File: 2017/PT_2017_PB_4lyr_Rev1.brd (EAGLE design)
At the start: 158.7 x 209.5 mm, 150 parts, among them Q12 2N7002

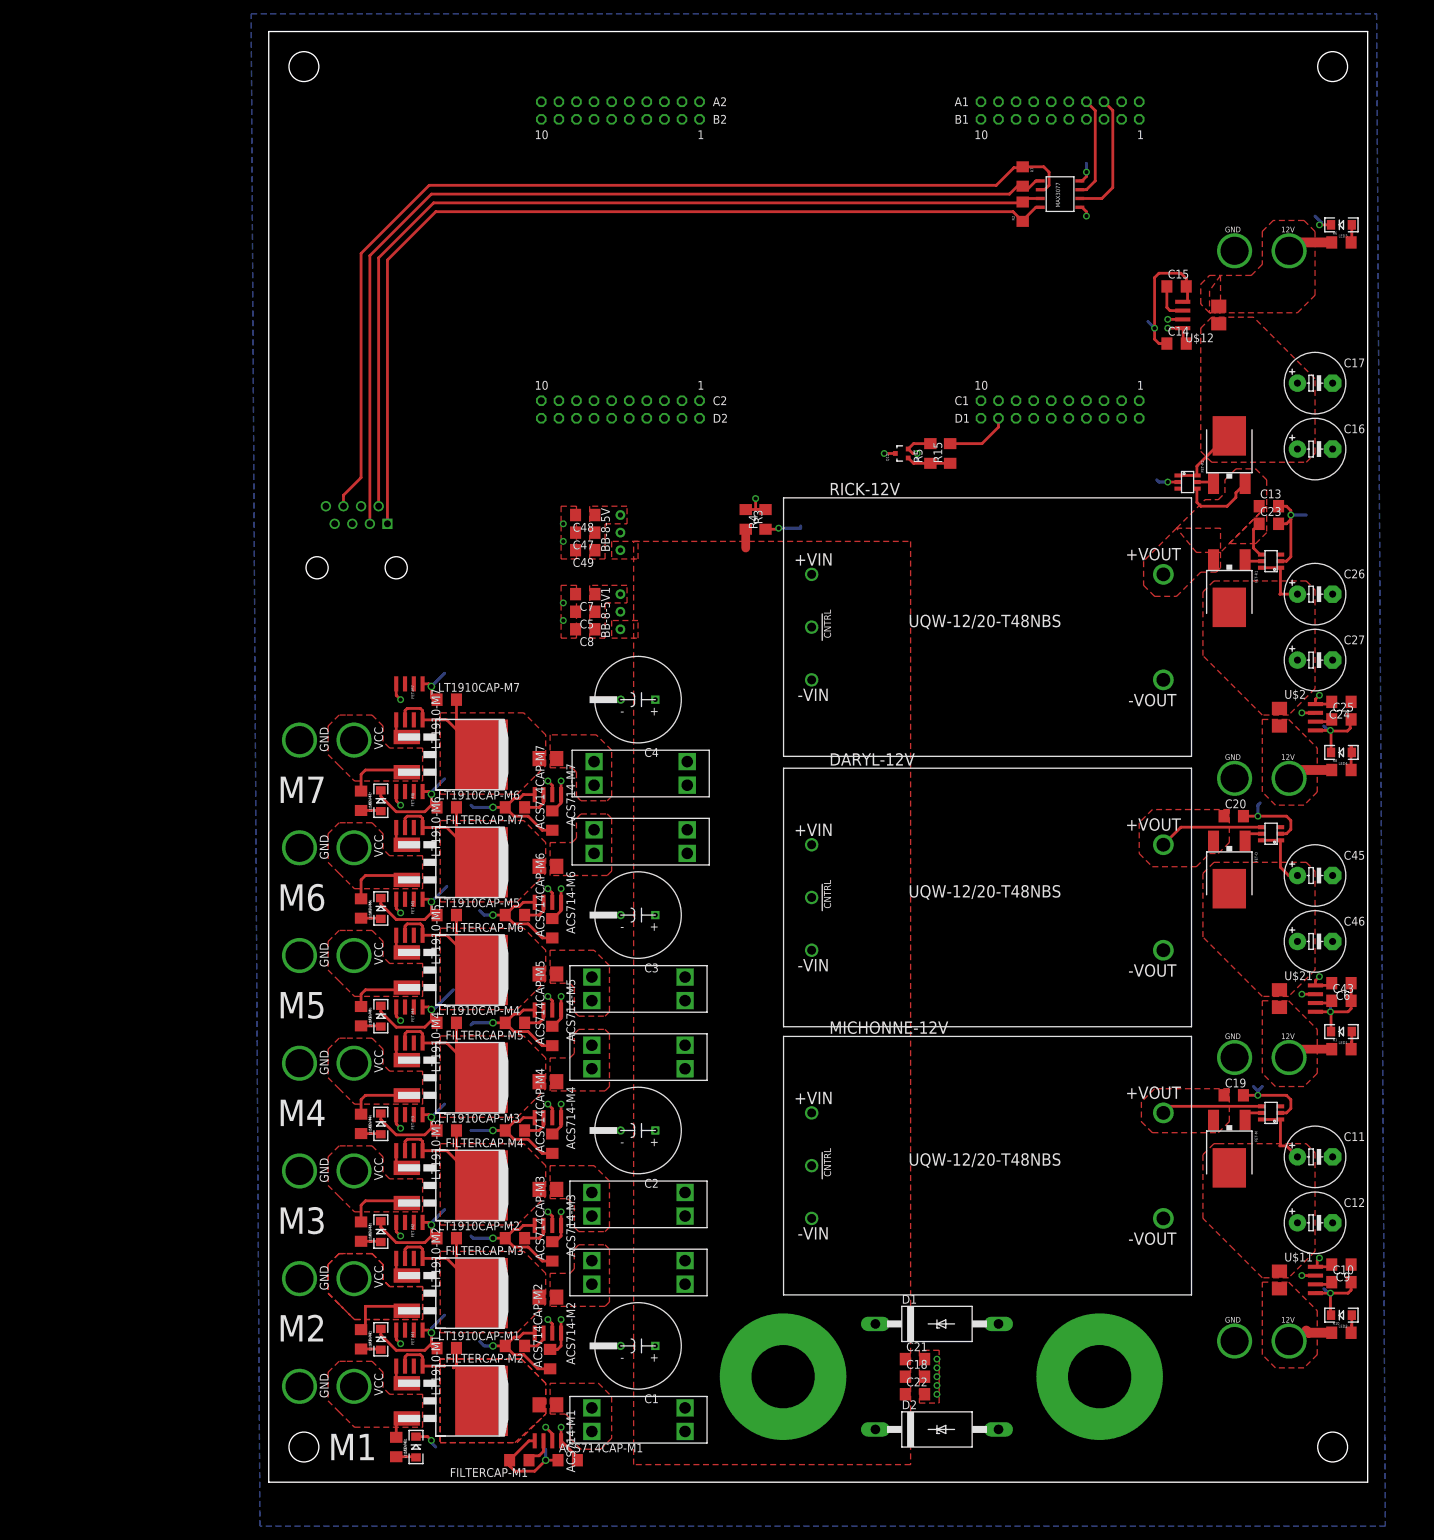
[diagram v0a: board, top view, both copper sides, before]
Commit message: Added fuse blocks and bus bar mounting holes
Fuse blocks for the 12V buses. Swapped temporary anderson connectors
with holes to mount bus bars to connect PB to patch panel.
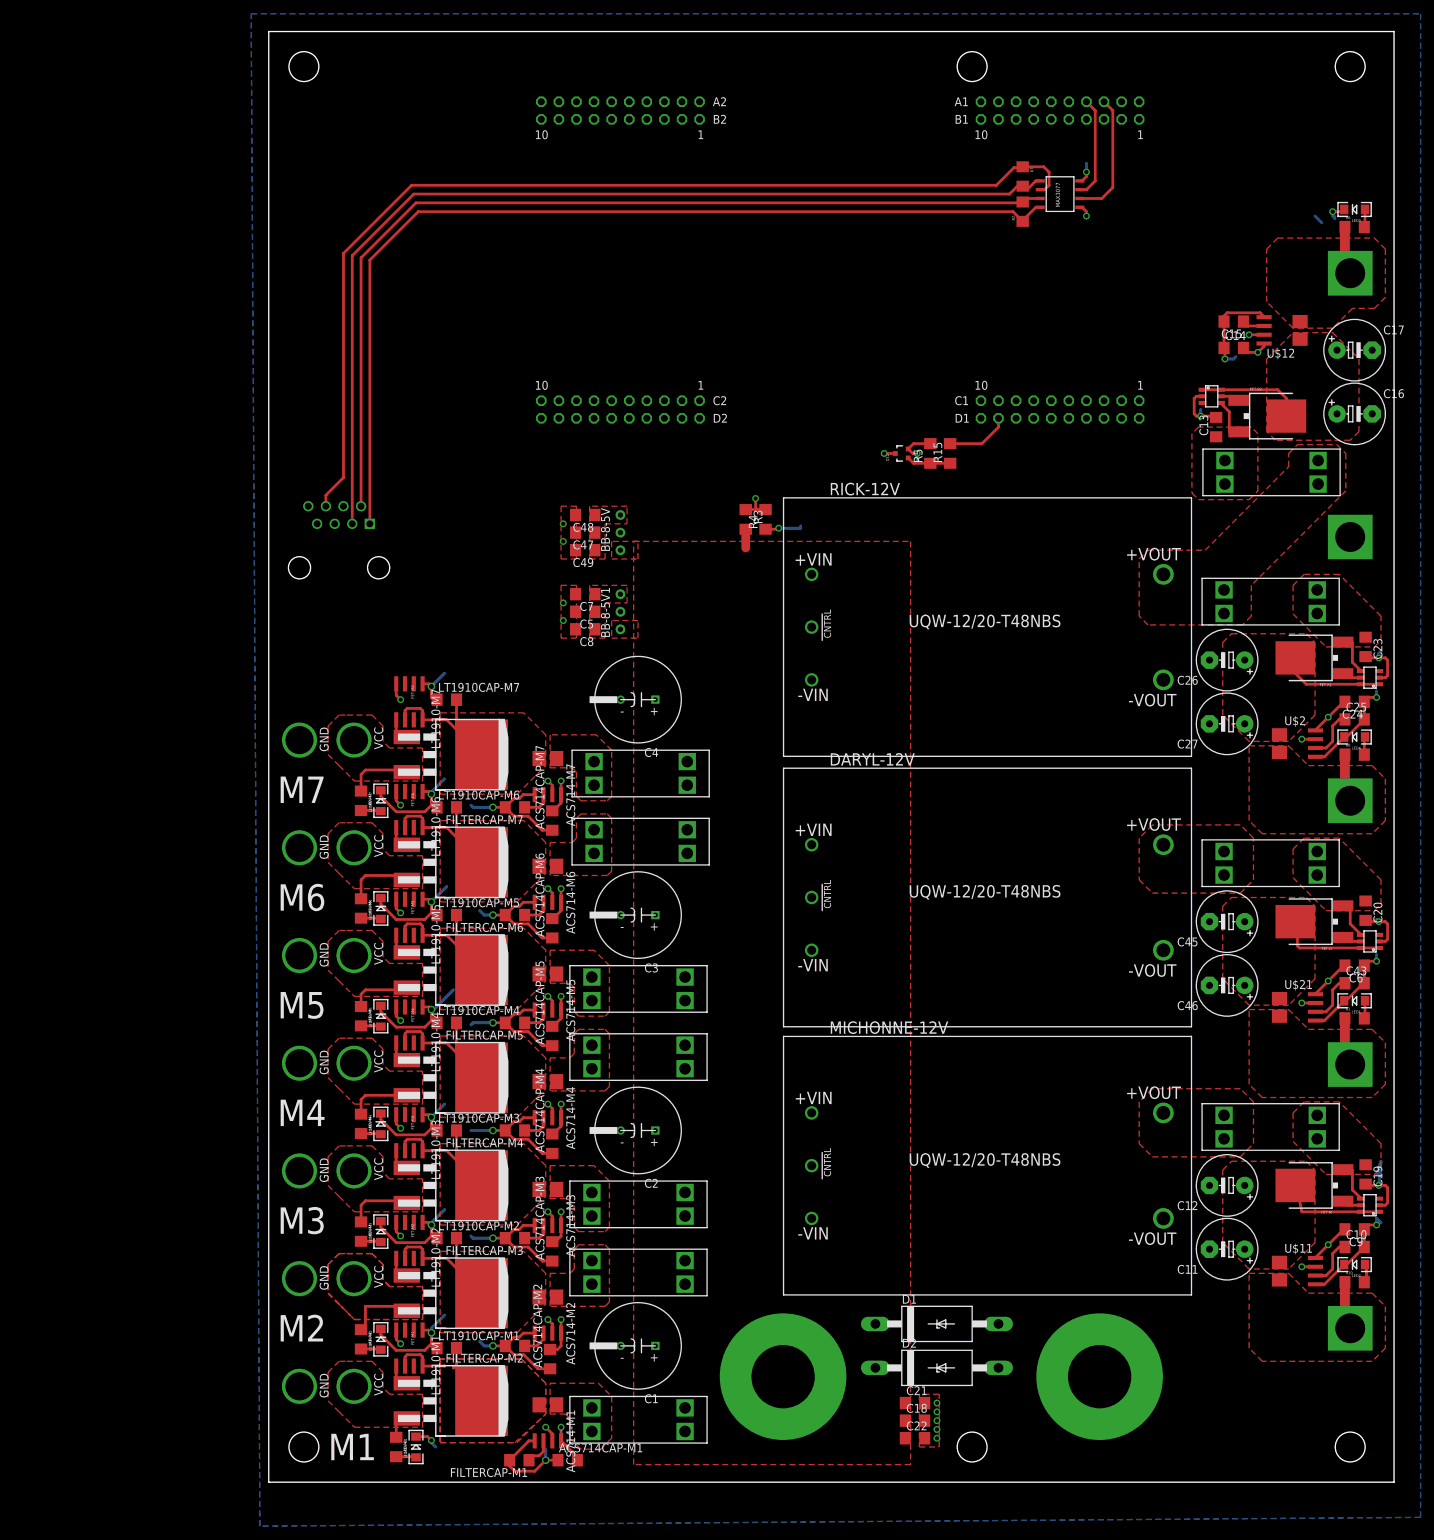
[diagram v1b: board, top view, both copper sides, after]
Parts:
- added U$14, U$30, U$31, U$32: ATC_FUSE_BLOCK, MRDT-Hardware:3557-2
- added U$33: BUS_BAR_MOUNTING_HOLE, MRDT-Connectors:1/8IN_BUS_BAR
- added U$34, U$35: MOUNTING_HOLE#8, MRDT-Hardware:#8_SCREW
- U$16, U$17, U$18, U$25: value APP_2POS_CONFIG12V_VERT -> BUS_BAR_MOUNTING_HOLE; device MRDT-Connectors:APP45_12V_VERT_CONFIG -> MRDT-Connectors:1/8IN_BUS_BAR
- moved U$18 161.7 mm to (156.2, 22.2), turned to 0 degrees
- moved U$16 151.0 mm to (156.2, 174.6), turned to 0 degrees
- moved U$25 36.5 mm to (156.2, 136.5), turned to 0 degrees
- moved C20 23.4 mm to (158.4, 82.5), turned to 270 degrees
- moved C23 22.6 mm to (158.4, 120.7), turned to 270 degrees
- moved C19 22.2 mm to (158.4, 44.5), turned to 270 degrees
- moved U$4 22.1 mm to (159.1, 116.2)
- moved U$17 21.4 mm to (156.2, 60.3), turned to 0 degrees
- moved U$6 21.1 mm to (159.1, 78.1)
- moved U$9 19.5 mm to (159.1, 40.0)
- moved C11 18.4 mm to (138.4, 33.7), turned to 180 degrees
- moved C26 15.9 mm to (138.4, 118.7), turned to 180 degrees
- moved C27 15.7 mm to (138.4, 109.5), turned to 180 degrees
- moved C45 14.3 mm to (138.4, 81.0), turned to 180 degrees
- moved FET-R1 14.2 mm to (149.9, 119.1), turned to 90 degrees
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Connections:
- new net N$18: RICK-12V.8, U$31.IN_1, U$31.IN_2, U$32.IN_1, U$32.IN_2
- new net N$21: DARYL-12V.8, U$30.IN_1, U$30.IN_2
- new net N$23: MICHONNE-12V.8, U$14.IN_1, U$14.IN_2
- new net N$9: C23.1, FET-R1.3, U$32.OUT_1, U$32.OUT_2, U$4.P$6
- net 12V-AUX-ACT: now also U$17.P$2; no longer U$17.VCC
- net 12V-AUX-ARM: now also U$18.P$2; no longer U$16.VCC
- net 12V-AUX-COM: now also U$33.P$2; no longer U$25.VCC
- net 12V-AUX-LOGIC: now also U$16.P$2; no longer U$18.VCC
- net GND: now also U$25.P$2; no longer U$16.GND, U$17.GND, U$18.GND, U$25.GND
- net N$1: now also U$30.OUT_1, U$30.OUT_2; no longer DARYL-12V.8
- net N$13: now also U$31.OUT_1, U$31.OUT_2; no longer C23.1, FET-R1.3, RICK-12V.8, U$4.P$6
- net N$2: now also U$14.OUT_1, U$14.OUT_2; no longer MICHONNE-12V.8
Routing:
- net 3.3V: track 76.0 -> 129.8 mm
- net LOGIC-12V-SIG: track 37.5 -> 48.7 mm
- net N$13: track 16.3 -> 6.00 mm
- net N$1: track 15.3 -> 5.63 mm
- net N$2: track 14.6 -> 6.00 mm
- net N$11: track 9.74 -> 17.6 mm
- net N$14: track 9.55 -> 15.6 mm
- net N$9: track 0.00 -> 6.00 mm
- net N$22: track 9.09 -> 15.0 mm
- net N$4: track 2.48 -> 7.27 mm
- net N$12: track 2.56 -> 7.27 mm
- net N$10: track 2.56 -> 7.27 mm
- net N$19: track 10.5 -> 15.2 mm
- net ARM-12V-SIG: track 197.9 -> 193.9 mm
- net 12V-AUX-ARM: track 3.81 -> 6.98 mm
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- added copper zone on layer 1, net N$18
- added copper zone on layer 1, net N$21
- added copper zone on layer 1, net N$23
- added copper zone on layer 1, net N$9
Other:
- board size 158.7 x 209.5 mm -> 162.5 x 209.5 mm

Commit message: Rearranged 5V & 3.3V Regulators
Also changed the horizontal RJ45 jack to a vertical jack.
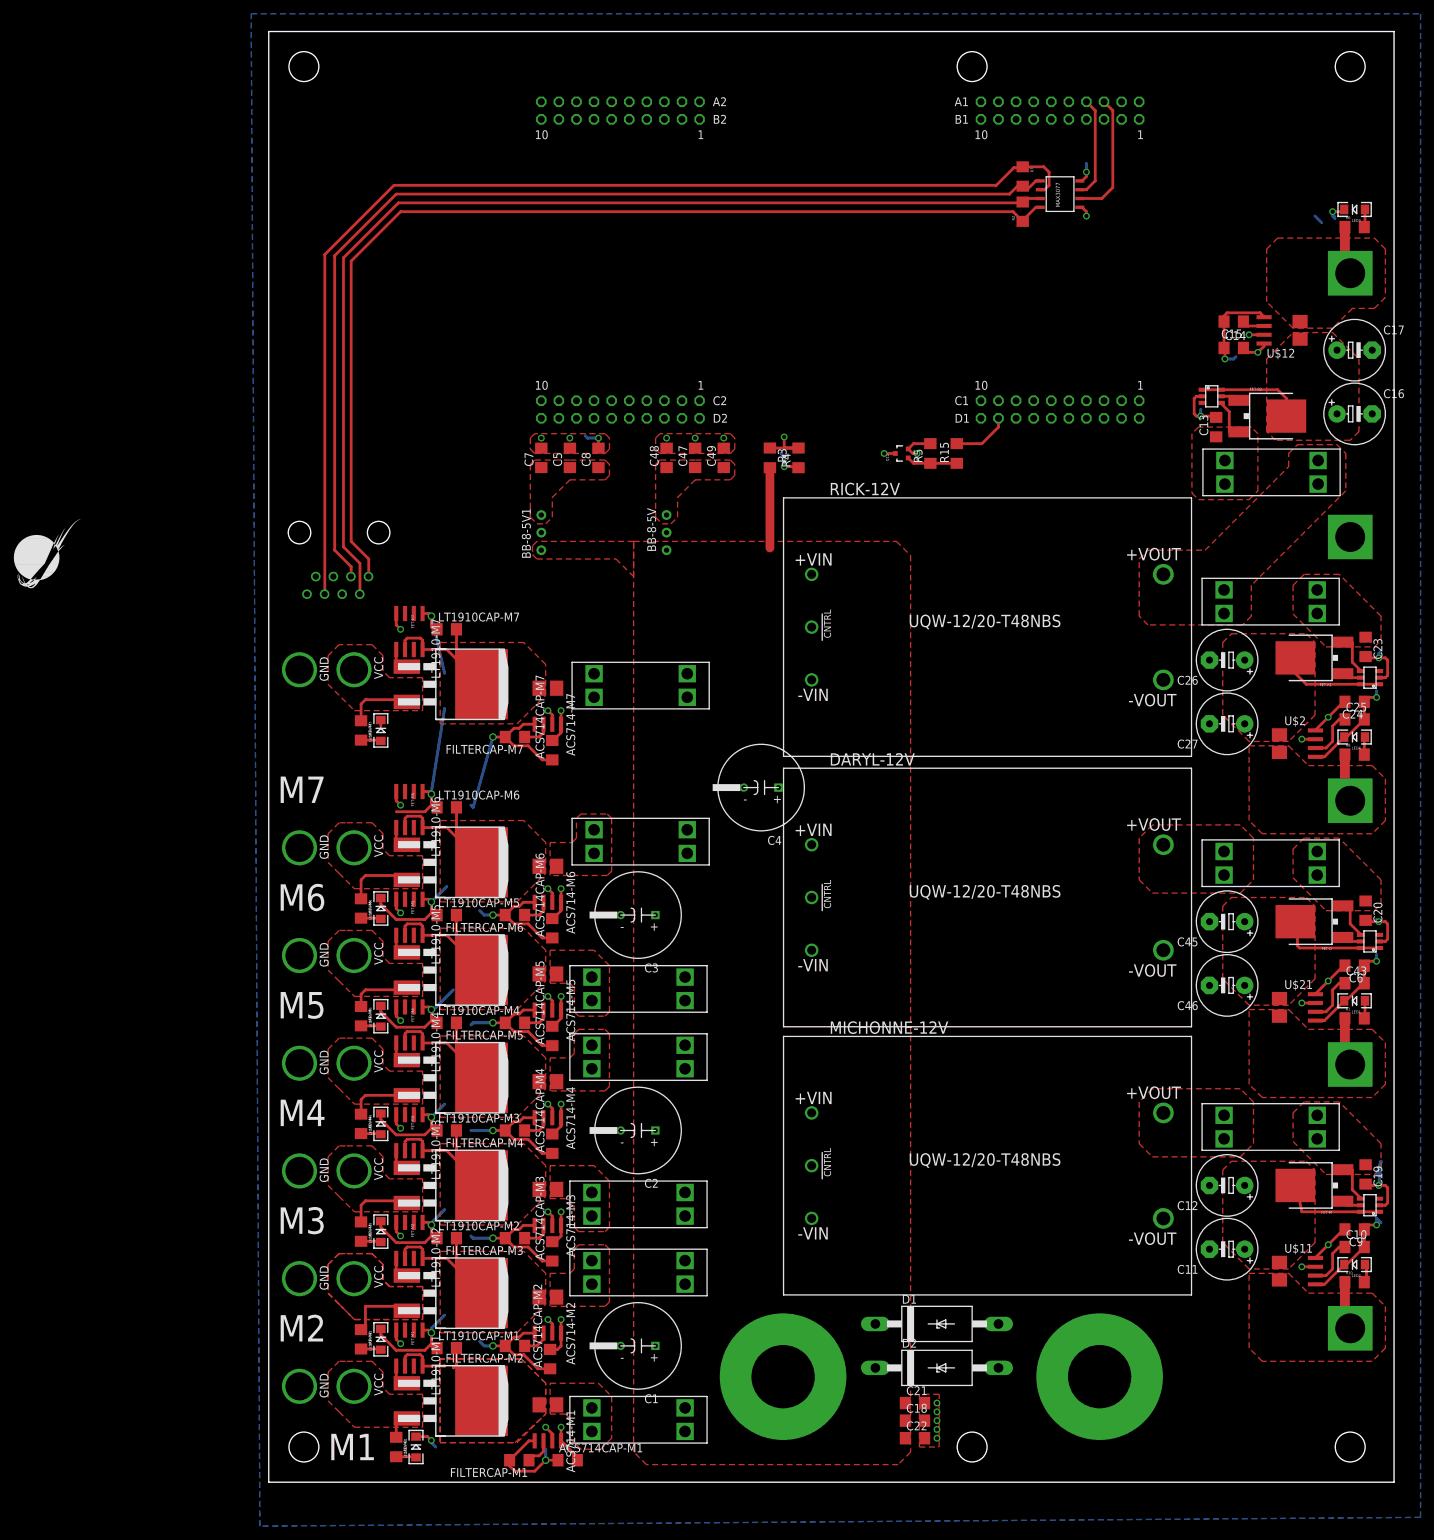
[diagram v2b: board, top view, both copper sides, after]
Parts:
- removed U$5: RJ45FCI-54602-908LF, MRDT-2015-General:FCI-54602-908LF
- added U$41: MRDT_LOGO, MRDT-2015-General:MRDT_LOGO
- added U$42: RJ45KEYSTONE-949, MRDT-2015-General:KEYSTONE-949
- moved C8 24.8 mm to (47.6, 148.0), turned to 90 degrees
- moved C49 24.0 mm to (65.7, 148.0), turned to 90 degrees
- moved C5 22.3 mm to (43.5, 148.0), turned to 90 degrees
- moved C4 21.8 mm to (71.1, 100.3)
- moved C7 20.7 mm to (39.4, 148.0), turned to 90 degrees
- moved C47 19.2 mm to (61.6, 148.0), turned to 90 degrees
- moved BB-8-5V1 16.2 mm to (39.4, 134.6)
- moved C48 14.4 mm to (57.5, 148.0), turned to 90 degrees
- moved U$28 12.7 mm to (43.8, 118.4)
- moved ACS714CAP-M7 10.2 mm to (41.0, 105.7)
- moved ACS714-M7 10.2 mm to (40.3, 112.1)
- moved FET-M7 10.2 mm to (24.1, 120.3)
- moved FILTERCAP-M7 10.2 mm to (35.6, 107.6)
- moved LED-M7 10.2 mm to (16.2, 108.6)
- moved LEDRES-M7 10.2 mm to (13.3, 108.6)
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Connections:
- net GND: now also U$42.P$7, U$42.P$8; no longer U$5.7, U$5.8
- net REC+1: now also U$42.P$1; no longer U$5.1
- net REC-1: now also U$42.P$2; no longer U$5.2
- net TRANS+1: now also U$42.P$3; no longer U$5.3
- net TRANS-1: now also U$42.P$6; no longer U$5.6
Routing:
- net GND: track 350.5 -> 372.5 mm, vias 36 -> 38
- net REC-1: track 137.6 -> 153.9 mm
- net TRANS-1: track 148.4 -> 162.7 mm
- net REC+1: track 139.3 -> 150.6 mm
- net TRANS+1: track 143.1 -> 154.3 mm
- net VMEAS-VBATT: track 98.7 -> 87.6 mm
- net IMEAS-M7: track 123.6 -> 113.4 mm
- net V_BATT: track 2.71 -> 11.6 mm
- net 3.3V: track 129.8 -> 138.7 mm
- net SIG-M7: track 59.2 -> 65.8 mm
- net SIG-12V: track 9.24 -> 8.29 mm
- net N$114: track 6.38 -> 7.33 mm
- net 5V: track 150.3 -> 151.2 mm
- removed copper zone on layer 1, net V_BATT_M7
